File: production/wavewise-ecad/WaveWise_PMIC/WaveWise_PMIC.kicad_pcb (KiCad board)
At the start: 2 copper layers, 1 part

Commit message: Started PCB
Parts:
- removed D**: ZLDO1117K50TC, SBR10200CTL-13:ZLDO1117K50TC
- added C1: 100u/80V, Capacitor_THT:CP_Radial_D10.0mm_P5.00mm, F.Cu at (94.0, 28.8)
- added C2: 1uF/100V, Capacitor_THT:C_Rect_L7.0mm_W2.5mm_P5.00mm, F.Cu at (208.3, 45.7)
- added C4: 2.2u/100V, Capacitor_SMD:C_1210_3225Metric_Pad1.33x2.70mm_HandSolder, F.Cu at (141.1, 22.9)
- added C5: 100n/25V, Capacitor_SMD:C_0402_1005Metric_Pad0.74x0.62mm_HandSolder, F.Cu at (147.3, 30.5)
- added C6: 1000u/10V, Capacitor_THT:CP_Radial_D10.0mm_P5.00mm, F.Cu at (118.3, 31.3)
- added C8: 560p/50V, Capacitor_SMD:C_0805_2012Metric_Pad1.18x1.45mm_HandSolder, F.Cu at (137.2, 30.5)
- added C9: 120u/50V, Capacitor_THT:CP_Radial_D8.0mm_P5.00mm, F.Cu at (139.5, 45.7)
- added D1: 1N5822, Diode_THT:D_DO-201AD_P15.24mm_Horizontal, F.Cu at (98.0, 51.7)
- added D2: 1N5817, Diode_THT:D_DO-41_SOD81_P10.16mm_Horizontal, F.Cu at (185.4, 38.1)
- added D3: SBR10200CTL-13, SBR10200CTL-13:ZLDO1117K50TC, F.Cu at (154.9, 27.3)
- added IC1: LV14360PDDAR, LV14360PDDAR:SOIC127P600X170-9N, F.Cu at (142.2, 30.5)
- added K1: Relay_SPDT, Relay_THT:Relay_SPDT_Finder_36.11, F.Cu at (190.1, 33.0)
- added L1: 100u, Inductor_SMD:L_12x12mm_H6mm, F.Cu at (105.6, 39.0)
- added L3: 27u, Inductor_SMD:L_12x12mm_H6mm, F.Cu at (149.9, 43.2)
- added Q2: 2N2219, Package_TO_SOT_THT:TO-92_Inline_Wide, F.Cu at (188.0, 20.3)
- added R1: 340k, Resistor_SMD:R_1206_3216Metric_Pad1.30x1.75mm_HandSolder, F.Cu at (76.2, 43.2)
- added R10: 0, Resistor_SMD:R_0805_2012Metric, F.Cu at (24.5, 76.2)
- added R11: 0, Resistor_SMD:R_0805_2012Metric, F.Cu at (24.5, 79.2)
- added R14: 45.3k, Resistor_SMD:R_0805_2012Metric_Pad1.20x1.40mm_HandSolder, F.Cu at (137.2, 26.4)
- added R2: 20k, Resistor_SMD:R_1206_3216Metric_Pad1.30x1.75mm_HandSolder, F.Cu at (68.6, 43.2)
- added R3: 500k, Resistor_SMD:R_1206_3216Metric_Pad1.30x1.75mm_HandSolder, F.Cu at (76.2, 48.3)
- added R4: 17k, Resistor_SMD:R_1206_3216Metric_Pad1.30x1.75mm_HandSolder, F.Cu at (67.6, 48.3)
- added R5: 10k, Resistor_SMD:R_0805_2012Metric_Pad1.20x1.40mm_HandSolder, F.Cu at (23.9, 88.9)
- added R6: 316k, Resistor_SMD:R_0805_2012Metric_Pad1.20x1.40mm_HandSolder, F.Cu at (138.2, 35.6)
- added R7: 50, Resistor_THT:R_Axial_DIN0516_L15.5mm_D5.0mm_P20.32mm_Horizontal, F.Cu at (213.4, 43.2)
- added R8: 5k, Resistor_SMD:R_0805_2012Metric_Pad1.20x1.40mm_HandSolder, F.Cu at (184.4, 22.9)
- added R9: 10.2k, Resistor_SMD:R_0805_2012Metric_Pad1.20x1.40mm_HandSolder, F.Cu at (132.1, 28.9)
- added U4: LM2576HVS-5.0_NOPB, Package_TO_SOT_SMD:TO-263-5_TabPin3, F.Cu at (105.8, 20.3)
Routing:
- net GND: track 0.00 -> 52.8 mm
- net +5V: track 0.00 -> 30.3 mm
- net /Connectors/Inverter_Input: track 0.00 -> 27.5 mm
- net Net-(D3-CATHODE): track 0.00 -> 27.0 mm
- net Net-(D1-K): track 0.00 -> 26.3 mm
- net +24V: track 0.00 -> 22.2 mm
- net +48V: track 0.00 -> 21.4 mm
- net Net-(D2-A): track 0.00 -> 14.1 mm
- net Net-(IC1-FB): track 0.00 -> 13.2 mm
- net Net-(Q2-B): track 0.00 -> 6.13 mm
- net Net-(C2-Pad1): track 0.00 -> 6.13 mm
- net /Panel_Sense: track 0.00 -> 5.51 mm
- net /BATT_SENS: track 0.00 -> 4.52 mm
- net Net-(IC1-RT/SYNC): track 0.00 -> 4.16 mm
- net Net-(IC1-BOOT): track 0.00 -> 4.06 mm

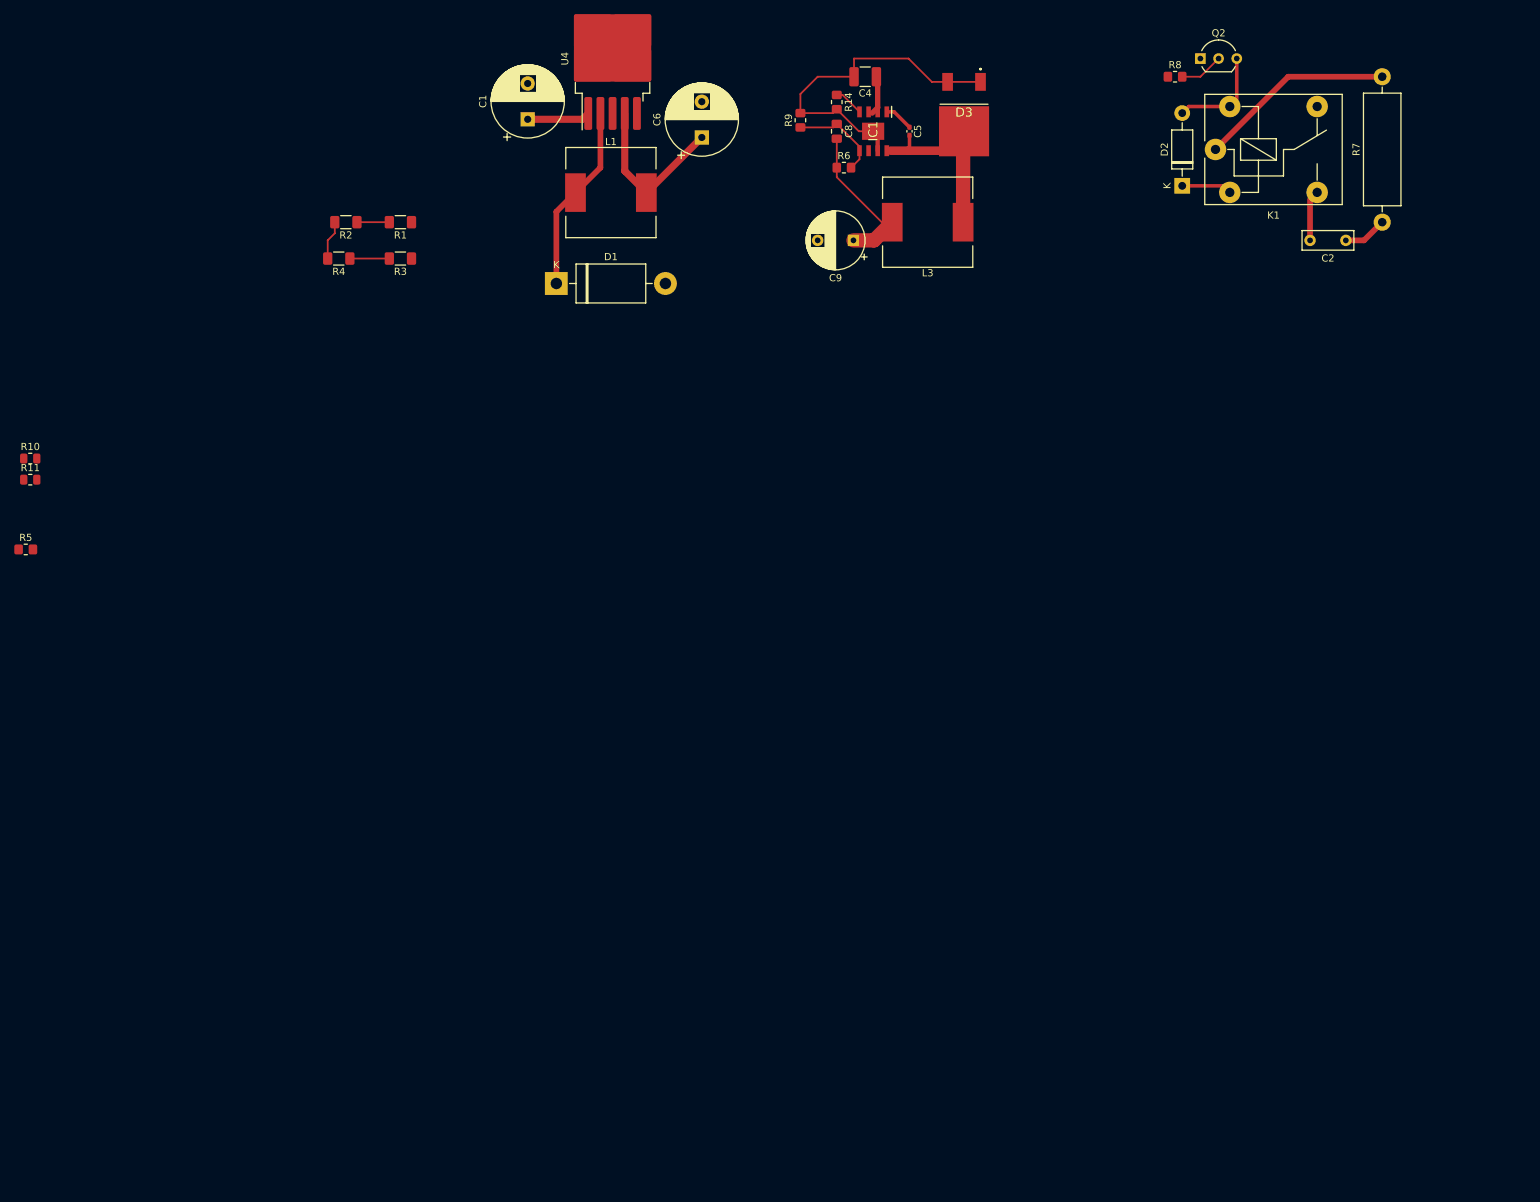
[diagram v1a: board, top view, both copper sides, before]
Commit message: added most footprints still need polulu footprint
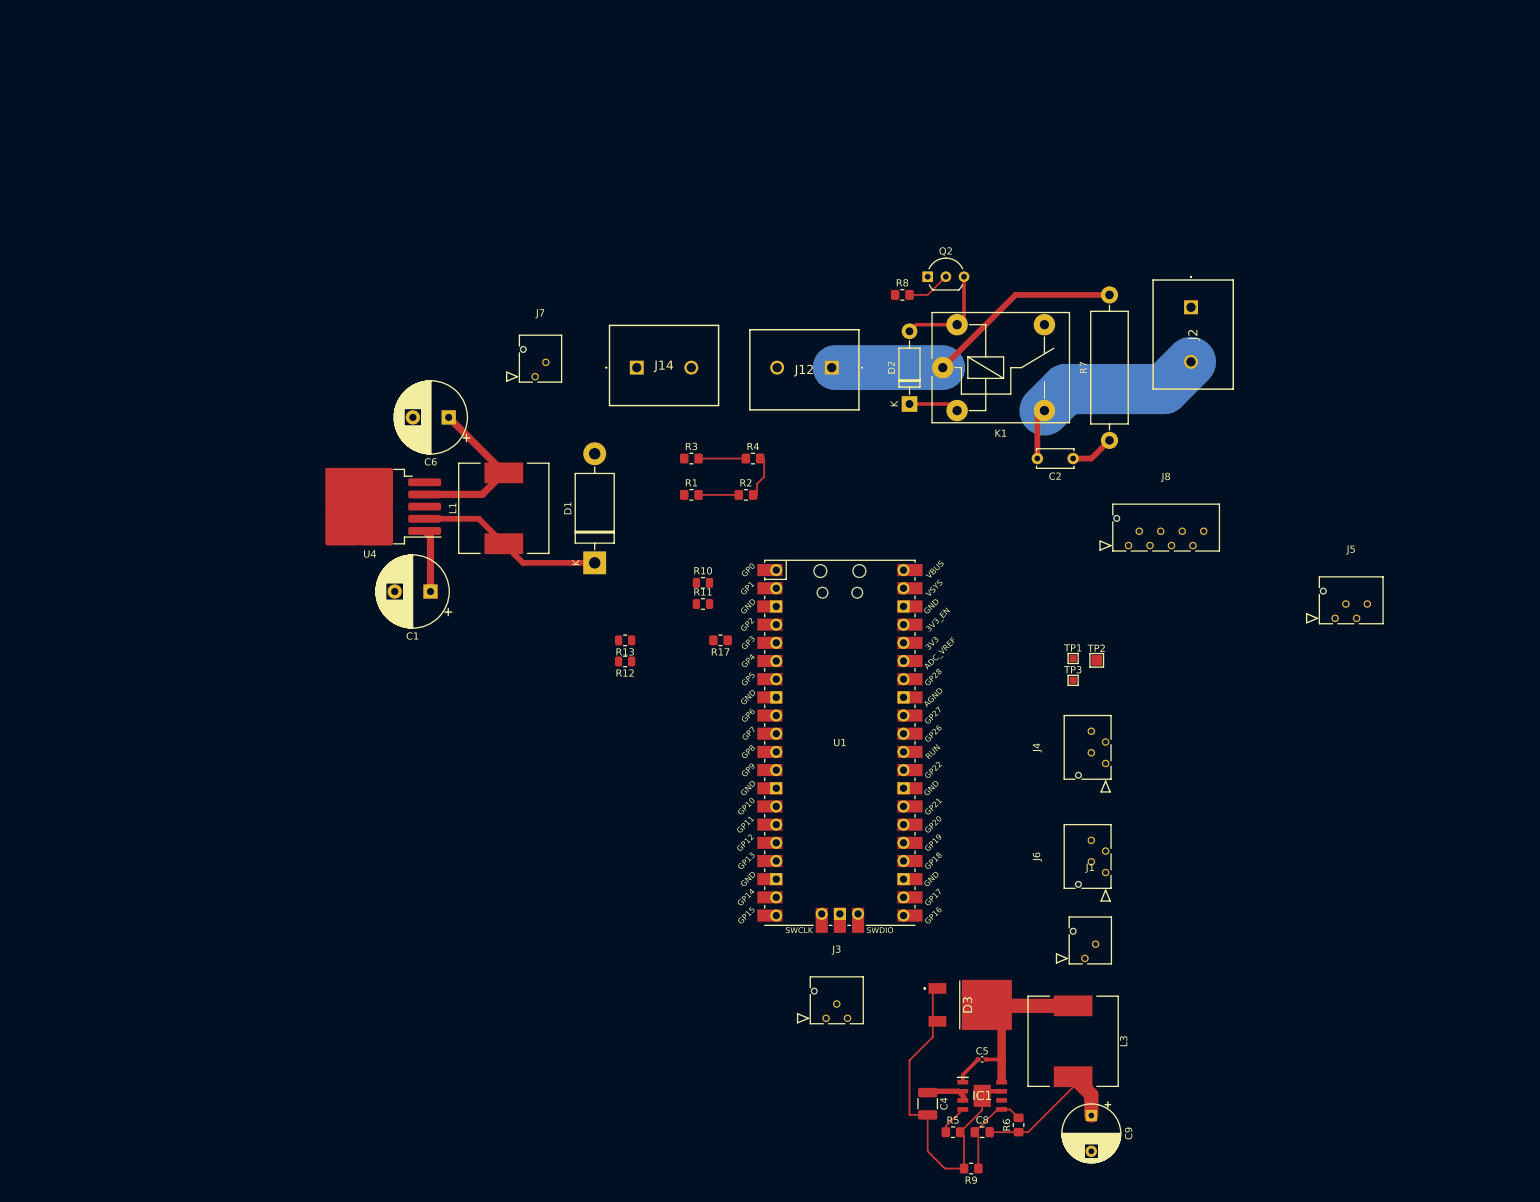
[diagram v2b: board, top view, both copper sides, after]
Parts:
- added J1: 24V output, Unchecked:2pinmolex, F.Cu at (171.8, 146.0)
- added J12: Regulated 48V Input, Unchecked:1731721, F.Cu at (136.4, 63.5)
- added J14: Battery Direct Input, Unchecked:1731721, F.Cu at (109.2, 63.5)
- added J2: Inverter Inputs, Unchecked:1731721, F.Cu at (186.7, 55.1)
- added J3: 5031590300, Unchecked:3pinmolex, F.Cu at (135.7, 154.4)
- added J4: 5031590400, Footprints:4pinmolex, F.Cu at (174.7, 118.8)
- added J5: 5031590400, Footprints:4pinmolex, F.Cu at (206.8, 98.5)
- added J6: 5031590400, Footprints:4pinmolex, F.Cu at (174.7, 134.0)
- added J7: 5V output, Unchecked:2pinmolex, F.Cu at (95.0, 64.8)
- added J8: 5031590800, Footprints:8pinmolex, F.Cu at (177.9, 88.4)
- added R12: 0, Resistor_SMD:R_0805_2012Metric, F.Cu at (107.6, 104.5)
- added R13: 0, Resistor_SMD:R_0805_2012Metric, F.Cu at (107.6, 101.6)
- added TP1: TestPoint, TestPoint:TestPoint_Pad_1.0x1.0mm, F.Cu at (170.2, 104.1)
- added TP2: TestPoint, TestPoint:TestPoint_Pad_1.5x1.5mm, F.Cu at (173.5, 104.4)
- added TP3: TestPoint, TestPoint:TestPoint_Pad_1.0x1.0mm, F.Cu at (170.2, 107.2)
- added U1: Raspberry Pi Pico, Unchecked:Pico, F.Cu at (137.6, 115.9)
- C2: footprint Capacitor_THT:C_Rect_L7.0mm_W2.5mm_P5.00mm -> Capacitor_THT:C_Disc_D5.0mm_W2.5mm_P5.00mm
- K1: value Relay_SPDT -> Relay_SPST-NO
- R1, R2, R3, R4: footprint Resistor_SMD:R_1206_3216Metric_Pad1.30x1.75mm_HandSolder -> Resistor_SMD:R_0805_2012Metric_Pad1.20x1.40mm_HandSolder
- moved R9 148.4 mm to (155.9, 175.4), turned to 180 degrees
- moved R5 144.8 mm to (153.4, 170.3), turned to 0 degrees
- moved C4 143.7 mm to (149.9, 166.3), turned to -90 degrees
- moved C8 141.3 mm to (157.5, 170.3), turned to 0 degrees
- moved R6 136.0 mm to (162.6, 169.3), turned to 90 degrees
- moved IC1 135.6 mm to (157.5, 165.2), turned to 0 degrees
- moved C5 130.1 mm to (157.5, 160.2), turned to 0 degrees
- moved C9 126.7 mm to (172.7, 168.0), turned to -90 degrees
- moved D3 125.2 mm to (154.9, 152.5), turned to -90 degrees
- moved L3 116.2 mm to (170.2, 157.6), turned to -90 degrees
- moved R17 97.9 mm to (120.9, 101.6), turned to 180 degrees
- moved R10 95.6 mm to (118.5, 93.6)
- moved R11 95.6 mm to (118.5, 96.5)
- moved U4 71.2 mm to (71.9, 82.9), turned to 180 degrees
- moved R2 67.6 mm to (124.5, 81.3), turned to 0 degrees
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- renumbered R5 to R17, R14 to R5
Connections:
- C2 pad 2: +48V -> /Connectors/Inverter_Input
- C6 pad 1: +5V -> (no net)
- C6 pad 2: GND -> (no net)
- C9 pad 1: +24V -> (no net)
- C9 pad 2: GND -> (no net)
- D2 pad 1: +5V -> +12V
- K1 pad 11: /Connectors/Inverter_Input -> +48V
- K1 pad 12: unconnected-(K1-Pad12) -> (no net)
- K1 pad 14: +48V -> /Connectors/Inverter_Input
- K1 pad A1: +5V -> +12V
- R10 pad 1: unconnected-(R10-Pad1) -> batt_sense
- R10 pad 2: /Connectors/dio_batt_sense -> /DIO_BatterySense
- R11 pad 1: unconnected-(R11-Pad1) -> batt_sense
- R11 pad 2: /Connectors/analog_batt_sense -> /BATT_SENS
- R7 pad 2: /Connectors/Inverter_Input -> +48V
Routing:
- net +48V: track 21.4 -> 57.5 mm
- net +5V: track 30.3 -> 23.2 mm
- net +12V: track 0.00 -> 7.03 mm
- net /Connectors/Inverter_Input: track 27.5 -> 30.4 mm
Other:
- copper layers 2 -> 4

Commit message: More stuff done to PCB Added polulu
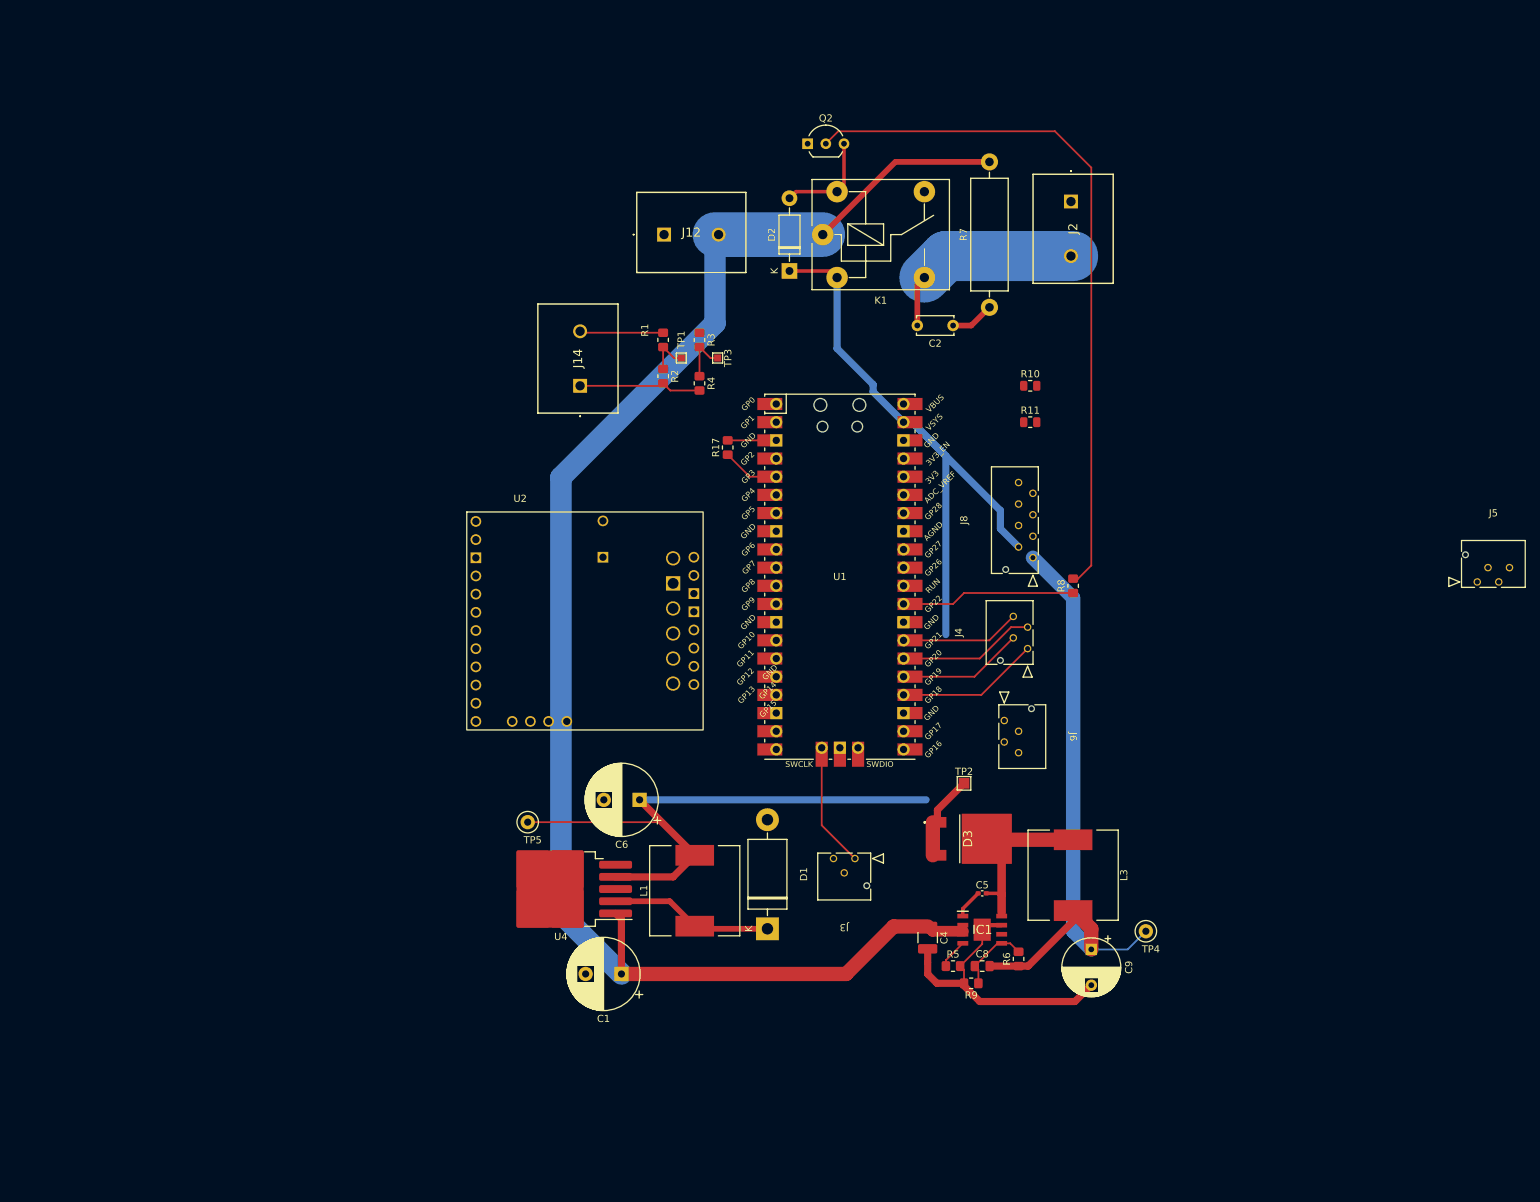
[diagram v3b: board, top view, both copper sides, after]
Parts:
- removed J1: 24V output, Unchecked:2pinmolex
- removed J7: 5V output, Unchecked:2pinmolex
- removed R12, R13: 0, Resistor_SMD:R_0805_2012Metric
- added TP4: 24V TP, TestPoint:TestPoint_Loop_D1.80mm_Drill1.0mm_Beaded, F.Cu at (180.3, 142.2)
- added TP5: 5V TP, TestPoint:TestPoint_Loop_D1.80mm_Drill1.0mm_Beaded, F.Cu at (94.0, 127.0)
- added U2: Pololu_DRV8711_Motor_Driver, Unchecked:POLOLU_36v4, F.Cu at (82.8, 81.2)
- moved TP1 69.0 mm to (115.4, 62.2), turned to -90 degrees
- moved TP3 67.0 mm to (120.5, 62.2), turned to -90 degrees
- moved C1 59.7 mm to (107.1, 148.2)
- moved L1 59.7 mm to (117.3, 136.6)
- moved C6 59.7 mm to (109.6, 123.9)
- moved U4 59.7 mm to (98.6, 136.3)
- moved D1 56.5 mm to (127.5, 141.9)
- moved R10 53.4 mm to (164.2, 66.0)
- moved R11 52.3 mm to (164.2, 71.1)
- moved R8 47.1 mm to (170.2, 94.0), turned to 90 degrees
- moved J12 29.9 mm to (113.0, 44.9), turned to 0 degrees
- moved R17 27.0 mm to (121.9, 74.7), turned to 90 degrees
- moved R9 25.9 mm to (155.9, 149.5)
- moved J6 25.5 mm to (160.6, 112.8), turned to -90 degrees
- moved TP2 25.3 mm to (154.9, 121.6)
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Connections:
- D2 pad 1: +12V -> +5V
- K1 pad 11: +48V -> (no net)
- K1 pad A1: +12V -> +5V
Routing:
- net +48V: track 57.5 -> 218.9 mm
- net +5V: track 23.2 -> 177.2 mm
- net Net-(Q2-B): track 6.13 -> 98.8 mm
- net +24V: track 22.2 -> 89.0 mm
- net /PUMP_CTL: track 0.00 -> 24.3 mm
- net GND: track 52.8 -> 76.4 mm
- net /GPIO1: track 0.00 -> 20.0 mm
- net /GPIO3: track 0.00 -> 19.2 mm
- net /GPIO2: track 0.00 -> 17.6 mm
- net /CLK: track 0.00 -> 17.4 mm
- net /Connectors/DIO: track 0.00 -> 16.9 mm
- net /GPIO4: track 0.00 -> 16.7 mm
- net +BATT: track 0.00 -> 11.7 mm
- net /MOTOR_RESET: track 0.00 -> 8.06 mm
- net +12V: track 7.03 -> 0.00 mm
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- added copper zone on In1.Cu, net GND
